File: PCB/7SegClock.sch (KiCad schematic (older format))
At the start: 21 parts, among them CON1 USB-MINI-B, Q1 NPN, U1 P8X32A, U2 24LC256, U3 FT232RL, U4 DS3231, U5 TPS62172DSGT, X1 5mhz CRYSTAL

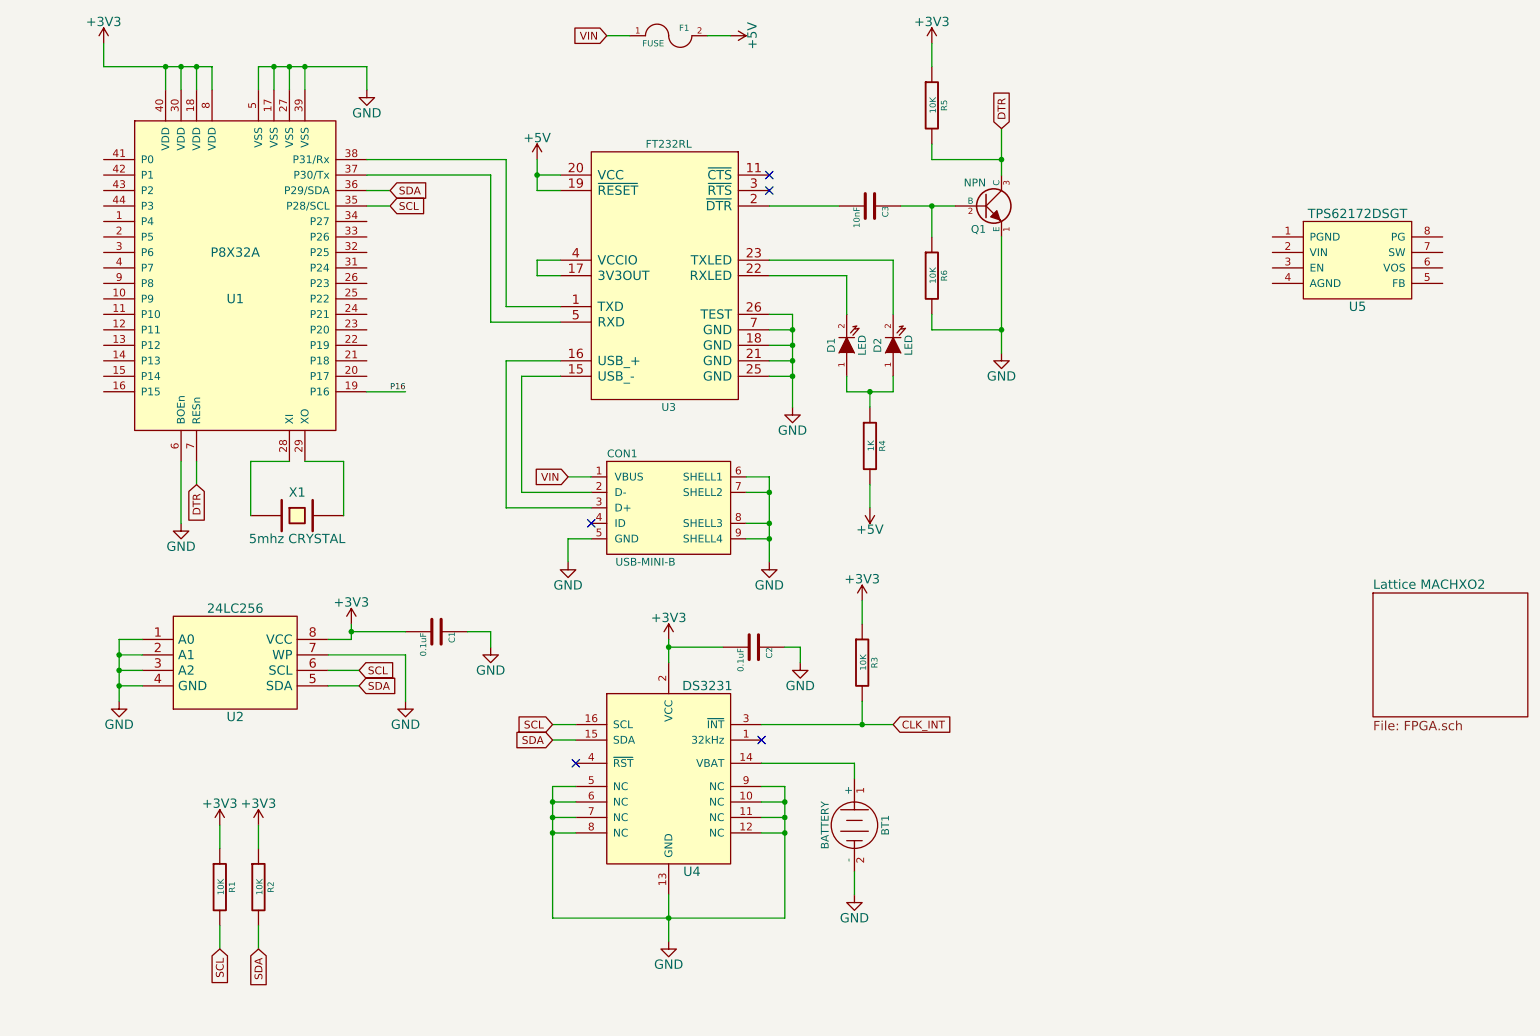
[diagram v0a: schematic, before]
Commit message: Worked on PCB, added FPGA.
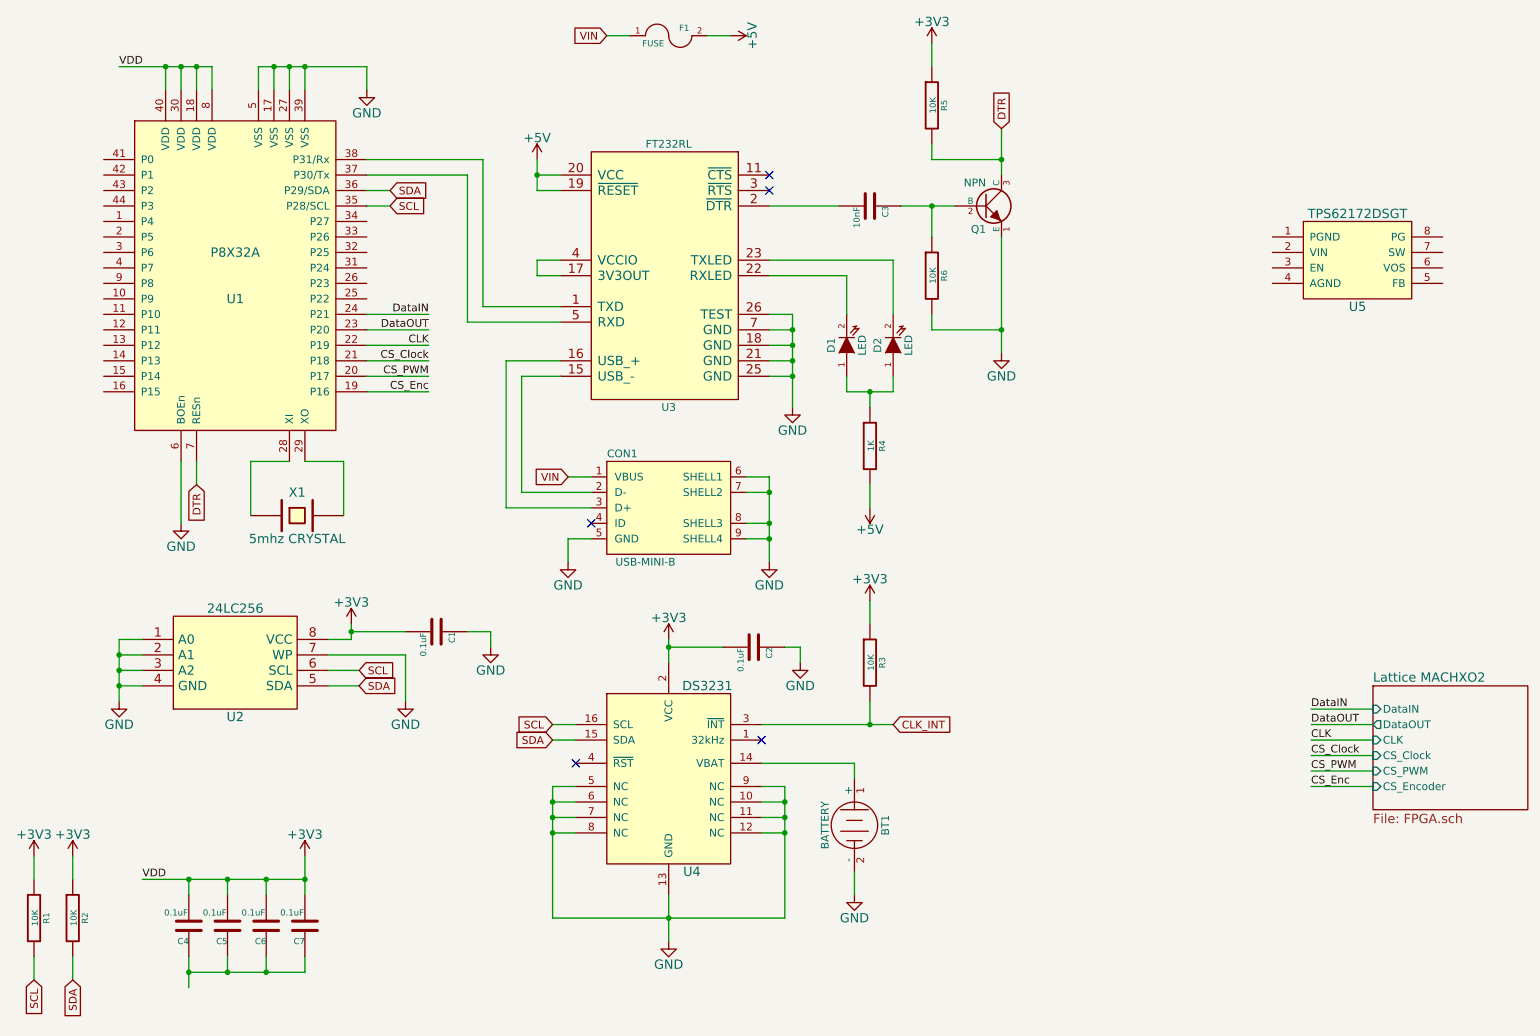
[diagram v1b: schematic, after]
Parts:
- added C4, C5, C6, C7: 0.1uF, Capacitors_SMD:C_0805_HandSoldering, symbol C
- U5: footprint (none) -> SMD_Packages:WSON-8-1EP
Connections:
- net +3V3: now also C4.2, C5.2, C6.2, C7.2
- net CS_PWM: now reaches U1.20 (P17)
- net CS_Clock: now reaches U1.21 (P18)
- net CLK: now reaches U1.22 (P19)
- net DataOUT: now reaches U1.23 (P20)
- net DataIN: now reaches U1.24 (P21)
- net P16 renamed CS_Enc
- new net: C4.1, C5.1, C6.1, C7.1
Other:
- moved on the sheet: R1, R2, R3

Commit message: Worked on PCB.
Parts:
- C1, C2, C3, C4, C5, C6, C7: footprint Capacitors_SMD:C_0805_HandSoldering -> Capacitors_SMD:C_0603_HandSoldering
- R1, R2, R3, R4, R5, R6: footprint Resistors_SMD:R_0805_HandSoldering -> Resistors_SMD:R_0603_HandSoldering
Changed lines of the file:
@@
 F 0 "C3" H 6350 2200 40  0000 L CNN
 F 1 "10nF" H 6356 2015 40  0000 L CNN
-F 2 "Capacitors_SMD:C_0805_HandSoldering" H 6388 1950 30  0001 C CNN
+F 2 "Capacitors_SMD:C_0603_HandSoldering" H 6388 1950 30  0001 C CNN
 F 3 "" H 6350 2100 60  0000 C CNN
 	1    6350 2100
@@
 F 0 "R6" V 6830 2550 40  0000 C CNN
 F 1 "10K" V 6757 2551 40  0000 C CNN
-F 2 "Resistors_SMD:R_0805_HandSoldering" V 6680 2550 30  0001 C CNN
+F 2 "Resistors_SMD:R_0603_HandSoldering" V 6680 2550 30  0001 C CNN
 F 3 "" H 6750 2550 30  0000 C CNN
 	1    6750 2550
@@
 F 0 "R5" V 6830 1450 40  0000 C CNN
 F 1 "10K" V 6757 1451 40  0000 C CNN
-F 2 "Resistors_SMD:R_0805_HandSoldering" V 6680 1450 30  0001 C CNN
+F 2 "Resistors_SMD:R_0603_HandSoldering" V 6680 1450 30  0001 C CNN
 F 3 "" H 6750 1450 30  0000 C CNN
 	1    6750 1450
@@
 F 0 "R4" V 6430 3650 40  0000 C CNN
 F 1 "1K" V 6357 3651 40  0000 C CNN
-F 2 "Resistors_SMD:R_0805_HandSoldering" V 6280 3650 30  0001 C CNN
+F 2 "Resistors_SMD:R_0603_HandSoldering" V 6280 3650 30  0001 C CNN
 F 3 "" H 6350 3650 30  0000 C CNN
 	1    6350 3650
@@
 F 0 "R2" V 1280 6700 40  0000 C CNN
 F 1 "10K" V 1207 6701 40  0000 C CNN
-F 2 "Resistors_SMD:R_0805_HandSoldering" V 1130 6700 30  0001 C CNN
+F 2 "Resistors_SMD:R_0603_HandSoldering" V 1130 6700 30  0001 C CNN
 F 3 "" H 1200 6700 30  0000 C CNN
 	1    1200 6700
@@
 F 0 "R1" V 1030 6700 40  0000 C CNN
 F 1 "10K" V 957 6701 40  0000 C CNN
-F 2 "Resistors_SMD:R_0805_HandSoldering" V 880 6700 30  0001 C CNN
+F 2 "Resistors_SMD:R_0603_HandSoldering" V 880 6700 30  0001 C CNN
 F 3 "" H 950 6700 30  0000 C CNN
 	1    950  6700
@@
 F 0 "C2" H 5600 5050 40  0000 L CNN
 F 1 "0.1uF" H 5606 4865 40  0000 L CNN
-F 2 "Capacitors_SMD:C_0805_HandSoldering" H 5638 4800 30  0001 C CNN
+F 2 "Capacitors_SMD:C_0603_HandSoldering" H 5638 4800 30  0001 C CNN
 F 3 "" H 5600 4950 60  0000 C CNN
 	1    5600 4950
@@
 F 0 "C1" H 3550 4950 40  0000 L CNN
 F 1 "0.1uF" H 3556 4765 40  0000 L CNN
-F 2 "Capacitors_SMD:C_0805_HandSoldering" H 3588 4700 30  0001 C CNN
+F 2 "Capacitors_SMD:C_0603_HandSoldering" H 3588 4700 30  0001 C CNN
 F 3 "" H 3550 4850 60  0000 C CNN
 	1    3550 4850
@@
 F 0 "R3" V 6430 5050 40  0000 C CNN
 F 1 "10K" V 6357 5051 40  0000 C CNN
-F 2 "Resistors_SMD:R_0805_HandSoldering" V 6280 5050 30  0001 C CNN
+F 2 "Resistors_SMD:R_0603_HandSoldering" V 6280 5050 30  0001 C CNN
 F 3 "" H 6350 5050 30  0000 C CNN
 	1    6350 5050
@@
 F 0 "C7" H 2700 6850 40  0000 L CNN
 F 1 "0.1uF" H 2706 6665 40  0000 L CNN
-F 2 "Capacitors_SMD:C_0805_HandSoldering" H 2738 6600 30  0001 C CNN
+F 2 "Capacitors_SMD:C_0603_HandSoldering" H 2738 6600 30  0001 C CNN
 F 3 "" H 2700 6750 60  0000 C CNN
 	1    2700 6750
@@
 F 0 "C6" H 2450 6850 40  0000 L CNN
 F 1 "0.1uF" H 2456 6665 40  0000 L CNN
-F 2 "Capacitors_SMD:C_0805_HandSoldering" H 2488 6600 30  0001 C CNN
+F 2 "Capacitors_SMD:C_0603_HandSoldering" H 2488 6600 30  0001 C CNN
 F 3 "" H 2450 6750 60  0000 C CNN
 	1    2450 6750
@@
 F 0 "C5" H 2200 6850 40  0000 L CNN
 F 1 "0.1uF" H 2206 6665 40  0000 L CNN
-F 2 "Capacitors_SMD:C_0805_HandSoldering" H 2238 6600 30  0001 C CNN
+F 2 "Capacitors_SMD:C_0603_HandSoldering" H 2238 6600 30  0001 C CNN
 F 3 "" H 2200 6750 60  0000 C CNN
 	1    2200 6750
@@
 F 0 "C4" H 1950 6850 40  0000 L CNN
 F 1 "0.1uF" H 1956 6665 40  0000 L CNN
-F 2 "Capacitors_SMD:C_0805_HandSoldering" H 1988 6600 30  0001 C CNN
+F 2 "Capacitors_SMD:C_0603_HandSoldering" H 1988 6600 30  0001 C CNN
 F 3 "" H 1950 6750 60  0000 C CNN
 	1    1950 6750

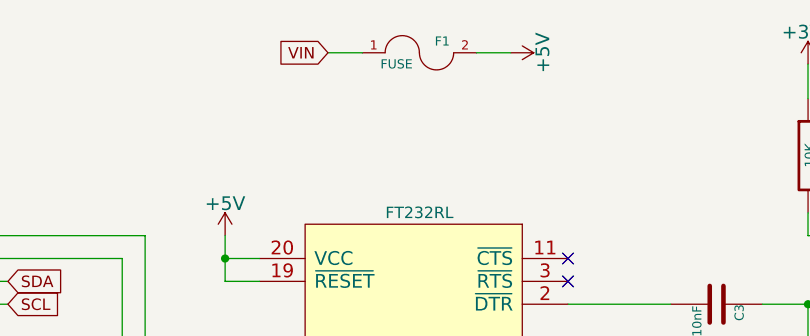
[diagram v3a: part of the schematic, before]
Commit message: Finished LED array footprint.
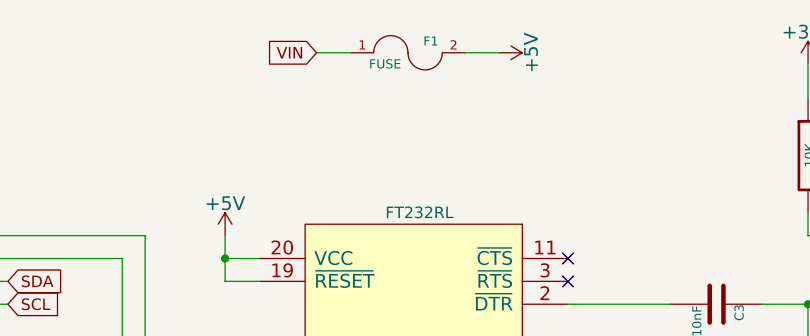
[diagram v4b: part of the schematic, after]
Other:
- moved on the sheet: F1
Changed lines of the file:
@@
 $Descr A4 11693 8268
 encoding utf-8
-Sheet 1 3
+Sheet 1 6
 Title "4 Digit 7 Segment Clock"
 Date "12/27/14"
@@
 L +5V #PWR06
 U 1 1 549F825B
-P 5450 1000
-F 0 "#PWR06" H 5450 850 60  0001 C CNN
-F 1 "+5V" H 5450 1140 60  0000 C CNN
-F 2 "" H 5450 1000 60  0000 C CNN
-F 3 "" H 5450 1000 60  0000 C CNN
-	1    5450 1000
+P 5400 1000
+F 0 "#PWR06" H 5400 850 60  0001 C CNN
+F 1 "+5V" H 5400 1140 60  0000 C CNN
+F 2 "" H 5400 1000 60  0000 C CNN
+F 3 "" H 5400 1000 60  0000 C CNN
+	1    5400 1000
 	0    1    1    0
 $EndComp
@@
 L FUSE F1
 U 1 1 54A0D025
-P 5050 1000
-F 0 "F1" H 5150 1050 40  0000 C CNN
-F 1 "FUSE" H 4950 950 40  0000 C CNN
-F 2 "" H 5050 1000 60  0001 C CNN
-F 3 "" H 5050 1000 60  0000 C CNN
-	1    5050 1000
+P 5000 1000
+F 0 "F1" H 5100 1050 40  0000 C CNN
+F 1 "FUSE" H 4900 950 40  0000 C CNN
+F 2 "" H 5000 1000 60  0001 C CNN
+F 3 "" H 5000 1000 60  0000 C CNN
+	1    5000 1000
 	1    0    0    -1
 $EndComp
@@
 $EndComp
 Wire Wire Line
-	5450 1000 5300 1000
-Text GLabel 4650 1000 0    50   Input ~ 0
+	5400 1000 5250 1000
+Text GLabel 4600 1000 0    50   Input ~ 0
 VIN
 Wire Wire Line
-	4800 1000 4650 1000
+	4750 1000 4600 1000
 Text GLabel 4400 3850 0    50   Input ~ 0
 VIN
